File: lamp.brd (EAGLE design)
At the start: 184.2 x 38.1 mm, 63 parts, among them P1 10kΩ, P2 2MΩ

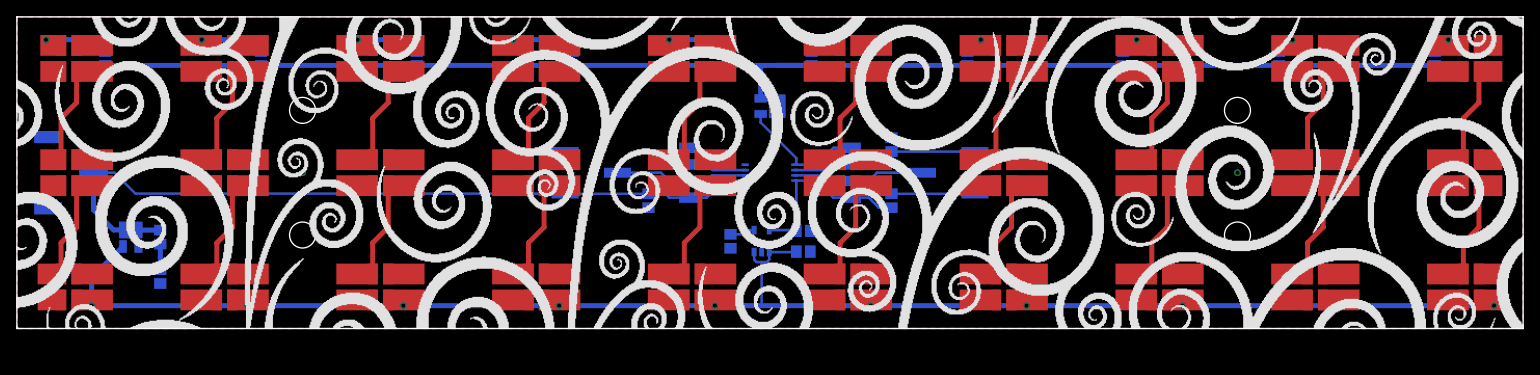
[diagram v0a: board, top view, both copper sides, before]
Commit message: Fixed nfet that controls led channels. Added resistors to pwm control line. Adjusted nfet and pfet symbols.
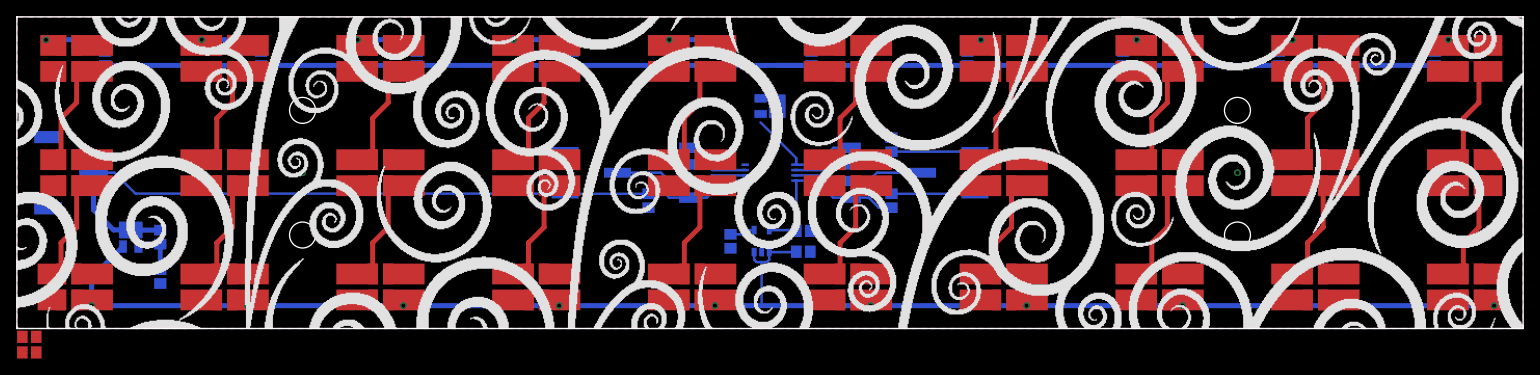
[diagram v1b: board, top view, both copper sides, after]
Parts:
- added R14: 100Ω, Barebones-Arduino:0805
- added R15: 100kΩ, Barebones-Arduino:0805
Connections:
- new net N$15: F1.P$1, R14.2, R15.2
- net GND: now also F1.S$2, R15.1; no longer F1.P$3
- net N$33: now also F1.P$3; no longer F1.S$2
- net N$47: now also R14.1; no longer F1.P$1
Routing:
- net N$33: track 170.7 -> 166.7 mm
- net N$47: track 15.8 -> 14.8 mm
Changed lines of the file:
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@@
 <layer number="29" name="tStop" color="7" fill="3" visible="yes" active="yes"/>
 <layer number="30" name="bStop" color="7" fill="6" visible="yes" active="yes"/>
-<layer number="31" name="tCream" color="7" fill="4" visible="no" active="yes"/>
-<layer number="32" name="bCream" color="7" fill="5" visible="no" active="yes"/>
+<layer number="31" name="tCream" color="7" fill="4" visible="yes" active="yes"/>
+<layer number="32" name="bCream" color="7" fill="5" visible="yes" active="yes"/>
 <layer number="33" name="tFinish" color="6" fill="3" visible="no" active="yes"/>
 <layer number="34" name="bFinish" color="6" fill="6" visible="no" active="yes"/>
@@
 </class>
 </classes>
-<designrules name="LaenPCBOrder *">
+<designrules name="LaenPCBOrder">
 <description language="de">&lt;b&gt;EAGLE Design Rules&lt;/b&gt;
 &lt;p&gt;
@@
 <param name="mvStopFrame" value="1"/>
 <param name="mvCreamFrame" value="0"/>
-<param name="mlMinStopFrame" value="5mil"/>
-<param name="mlMaxStopFrame" value="5mil"/>
+<param name="mlMinStopFrame" value="3mil"/>
+<param name="mlMaxStopFrame" value="3mil"/>
 <param name="mlMinCreamFrame" value="0mil"/>
 <param name="mlMaxCreamFrame" value="0mil"/>
-<param name="mlViaStopLimit" value="26mil"/>
+<param name="mlViaStopLimit" value="0mil"/>
 <param name="srRoundness" value="0"/>
 <param name="srMinRoundness" value="0mil"/>
@@
 <element name="C5" library=" Barebones-Arduino" package="0805" value="1µF" x="17.526" y="11.176" rot="MR270"/>
 <element name="F1" library="lamp" package="SOT-23-3" value="SI2318DS" x="92.075" y="27.178" smashed="yes" rot="MR90"/>
+<element name="R14" library=" Barebones-Arduino" package="0805" value="100Ω" x="1.524" y="-1.016"/>
+<element name="R15" library=" Barebones-Arduino" package="0805" value="100kΩ" x="1.524" y="-2.921"/>
 </elements>
 <signals>
@@
 <contactref element="U$3" pad="P$2"/>
 <wire x1="178.7525" y1="27.6225" x2="176.8475" y2="25.7175" width="0.6096" layer="1"/>
-<wire x1="176.8475" y1="20.6375" x2="176.8475" y2="25.7175" width="0.6096" layer="1"/>
+<wire x1="176.8475" y1="25.7175" x2="176.8475" y2="20.6375" width="0.6096" layer="1"/>
 <wire x1="178.7525" y1="27.6225" x2="178.7525" y2="31.4325" width="0.6096" layer="1"/>
 </signal>
@@
 <via x="155.956" y="35.306" extent="1-16" drill="0.5"/>
 <wire x1="157.7975" y1="35.306" x2="155.956" y2="35.306" width="0.6096" layer="1"/>
-<wire x1="157.7975" y1="34.6075" x2="157.7975" y2="35.306" width="0.6096" layer="1"/>
+<wire x1="157.7975" y1="35.306" x2="157.7975" y2="34.6075" width="0.6096" layer="1"/>
 </signal>
 <signal name="N$6">
@@
 <contactref element="U$8" pad="P$2"/>
 <wire x1="140.6525" y1="12.3825" x2="138.7475" y2="10.4775" width="0.6096" layer="1"/>
-<wire x1="138.7475" y1="10.4775" x2="138.7475" y2="6.6675" width="0.6096" layer="1"/>
+<wire x1="138.7475" y1="6.6675" x2="138.7475" y2="10.4775" width="0.6096" layer="1"/>
 <wire x1="140.6525" y1="12.3825" x2="140.6525" y2="17.4625" width="0.6096" layer="1"/>
 </signal>
@@
 <via x="136.906" y="35.306" extent="1-16" drill="0.5"/>
 <wire x1="138.7475" y1="35.306" x2="136.906" y2="35.306" width="0.6096" layer="1"/>
-<wire x1="138.7475" y1="34.6075" x2="138.7475" y2="35.306" width="0.6096" layer="1"/>
+<wire x1="138.7475" y1="35.306" x2="138.7475" y2="34.6075" width="0.6096" layer="1"/>
 </signal>
 <signal name="N$9">
@@
 <contactref element="U$9" pad="P$2"/>
 <wire x1="140.6525" y1="27.6225" x2="138.7475" y2="25.7175" width="0.6096" layer="1"/>
-<wire x1="138.7475" y1="20.6375" x2="138.7475" y2="25.7175" width="0.6096" layer="1"/>
+<wire x1="138.7475" y1="25.7175" x2="138.7475" y2="20.6375" width="0.6096" layer="1"/>
 <wire x1="140.6525" y1="27.6225" x2="140.6525" y2="31.4325" width="0.6096" layer="1"/>
 </signal>
@@
 <contactref element="U$11" pad="P$2"/>
 <wire x1="121.6025" y1="12.3825" x2="119.6975" y2="10.4775" width="0.6096" layer="1"/>
-<wire x1="121.6025" y1="17.4625" x2="121.6025" y2="12.3825" width="0.6096" layer="1"/>
+<wire x1="121.6025" y1="12.3825" x2="121.6025" y2="17.4625" width="0.6096" layer="1"/>
 <wire x1="119.6975" y1="10.4775" x2="119.6975" y2="6.6675" width="0.6096" layer="1"/>
 </signal>
@@
 <via x="117.856" y="35.306" extent="1-16" drill="0.5"/>
 <wire x1="119.6975" y1="35.306" x2="117.856" y2="35.306" width="0.6096" layer="1"/>
-<wire x1="119.6975" y1="34.6075" x2="119.6975" y2="35.306" width="0.6096" layer="1"/>
+<wire x1="119.6975" y1="35.306" x2="119.6975" y2="34.6075" width="0.6096" layer="1"/>
 </signal>
 <signal name="N$12">
@@
 <contactref element="U$14" pad="P$2"/>
 <wire x1="102.5525" y1="12.3825" x2="100.6475" y2="10.4775" width="0.6096" layer="1"/>
-<wire x1="102.5525" y1="17.4625" x2="102.5525" y2="12.3825" width="0.6096" layer="1"/>
 <wire x1="100.6475" y1="10.4775" x2="100.6475" y2="6.6675" width="0.6096" layer="1"/>
+<wire x1="102.5525" y1="12.3825" x2="102.5525" y2="17.4625" width="0.6096" layer="1"/>
 </signal>
 <signal name="N$32">
@@
 <via x="98.806" y="35.306" extent="1-16" drill="0.5"/>
 <wire x1="100.6475" y1="35.306" x2="98.806" y2="35.306" width="0.6096" layer="1"/>
-<wire x1="100.6475" y1="34.6075" x2="100.6475" y2="35.306" width="0.6096" layer="1"/>
+<wire x1="100.6475" y1="35.306" x2="100.6475" y2="34.6075" width="0.6096" layer="1"/>
 </signal>
 <signal name="N$13">
@@
 <contactref element="C4" pad="2"/>
 <contactref element="R13" pad="1"/>
-<contactref element="F1" pad="P$3"/>
 <contactref element="R12" pad="2"/>
+<contactref element="F1" pad="S$2"/>
+<contactref element="R15" pad="1"/>
+<wire x1="106.934" y1="23.329" x2="149.225" y2="19.05" width="0" layer="19" extent="16-16"/>
+<wire x1="96.989" y1="11.938" x2="106.934" y2="23.329" width="0" layer="19" extent="16-16"/>
+<wire x1="96.989" y1="9.398" x2="96.989" y2="11.938" width="0" layer="19" extent="16-16"/>
+<wire x1="91.059" y1="9.348" x2="96.989" y2="9.398" width="0" layer="19" extent="16-16"/>
+<wire x1="87.249" y1="9.818" x2="91.059" y2="9.348" width="0" layer="19" extent="16-16"/>
+<wire x1="89.045" y1="20.025" x2="87.249" y2="9.818" width="0" layer="19" extent="16-16"/>
+<wire x1="82.2325" y1="22.098" x2="89.045" y2="20.025" width="0" layer="19" extent="16-16"/>
+<wire x1="90.925" y1="28.128" x2="89.045" y2="20.025" width="0" layer="19" extent="16-16"/>
+<wire x1="77.216" y1="14.771" x2="82.2325" y2="22.098" width="0" layer="19" extent="16-16"/>
+<wire x1="34.925" y1="19.05" x2="77.216" y2="14.771" width="0" layer="19" extent="16-16"/>
+<wire x1="17.526" y1="5.5" x2="34.925" y2="19.05" width="0" layer="19" extent="16-16"/>
+<wire x1="9.37" y1="21.05" x2="17.526" y2="5.5" width="0" layer="19" extent="16-16"/>
+<wire x1="0.674" y1="-2.921" x2="17.526" y2="5.5" width="0" layer="19" extent="1-16"/>
 </signal>
 <signal name="N$18">
@@
 <contactref element="UC" pad="P$5"/>
 <contactref element="PB0" pad="1"/>
-<contactref element="F1" pad="P$1"/>
 <wire x1="101.9175" y1="22.098" x2="99.822" y2="22.098" width="0.3048" layer="16"/>
 <wire x1="99.822" y1="22.098" x2="97.749" y2="20.025" width="0.3048" layer="16"/>
@@
 <wire x1="95.289" y1="20.025" x2="95.289" y2="20.828" width="0.3048" layer="16"/>
 <wire x1="95.289" y1="20.828" x2="90.925" y2="25.192" width="0.3048" layer="16"/>
-<wire x1="90.925" y1="25.192" x2="90.925" y2="26.228" width="0.3048" layer="16"/>
+<contactref element="R14" pad="1"/>
+<wire x1="0.674" y1="-1.016" x2="90.925" y2="25.192" width="0" layer="19" extent="1-16"/>
 </signal>
 <signal name="N$46">
@@
 <wire x1="91.059" y1="8.128" x2="91.059" y2="2.794" width="0.3048" layer="16"/>
 <wire x1="91.059" y1="2.794" x2="88.9" y2="2.794" width="0.3048" layer="16"/>
+<wire x1="178.816" y1="3.429" x2="178.816" y2="2.794" width="0.6096" layer="1"/>
 <wire x1="102.5525" y1="3.4925" x2="102.5525" y2="2.794" width="0.6096" layer="1"/>
-<wire x1="159.7025" y1="3.4925" x2="159.7025" y2="2.794" width="0.6096" layer="1"/>
-<wire x1="140.6525" y1="3.4925" x2="140.6525" y2="2.794" width="0.6096" layer="1"/>
 <wire x1="121.6025" y1="3.4925" x2="121.6025" y2="2.794" width="0.6096" layer="1"/>
+<wire x1="140.6525" y1="3.4925" x2="140.6525" y2="2.794" width="0.6096" layer="1"/>
+<wire x1="159.7025" y1="3.4925" x2="159.7025" y2="2.794" width="0.6096" layer="1"/>
 <wire x1="178.7525" y1="3.4925" x2="178.816" y2="3.4925" width="0.6096" layer="1"/>
-<wire x1="178.816" y1="3.4925" x2="178.816" y2="2.794" width="0.6096" layer="1"/>
+<wire x1="178.816" y1="3.4925" x2="178.816" y2="3.429" width="0.6096" layer="1"/>
 </signal>
 <signal name="N$50">
@@
 <wire x1="90.925" y1="32.17" x2="86.995" y2="32.17" width="0.6096" layer="16"/>
 <wire x1="97.155" y1="32.17" x2="93.025" y2="32.17" width="0.6096" layer="16"/>
-<contactref element="F1" pad="S$2"/>
-<wire x1="90.925" y1="28.128" x2="90.925" y2="32.17" width="0.6096" layer="16"/>
 <wire x1="90.925" y1="32.17" x2="91.44" y2="32.17" width="0.6096" layer="16"/>
+<contactref element="F1" pad="P$3"/>
+<wire x1="93.025" y1="32.17" x2="92.95" y2="27.178" width="0" layer="19" extent="16-16"/>
 </signal>
 <signal name="+12V">
@@
 <wire x1="84.328" y1="20.066" x2="82.2325" y2="20.066" width="0.3048" layer="16"/>
 </signal>
+<signal name="N$15">
+<contactref element="R14" pad="2"/>
+<contactref element="R15" pad="2"/>
+<contactref element="F1" pad="P$1"/>
+<wire x1="2.374" y1="-1.016" x2="90.925" y2="26.228" width="0" layer="19" extent="1-16"/>
+<wire x1="2.374" y1="-2.921" x2="2.374" y2="-1.016" width="0" layer="19" extent="1-1"/>
+</signal>
 </signals>

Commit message: Removed soft-start RC from reverse polarity protection fet F2. Removed solder mask holes from led vias so they will get tented instead.
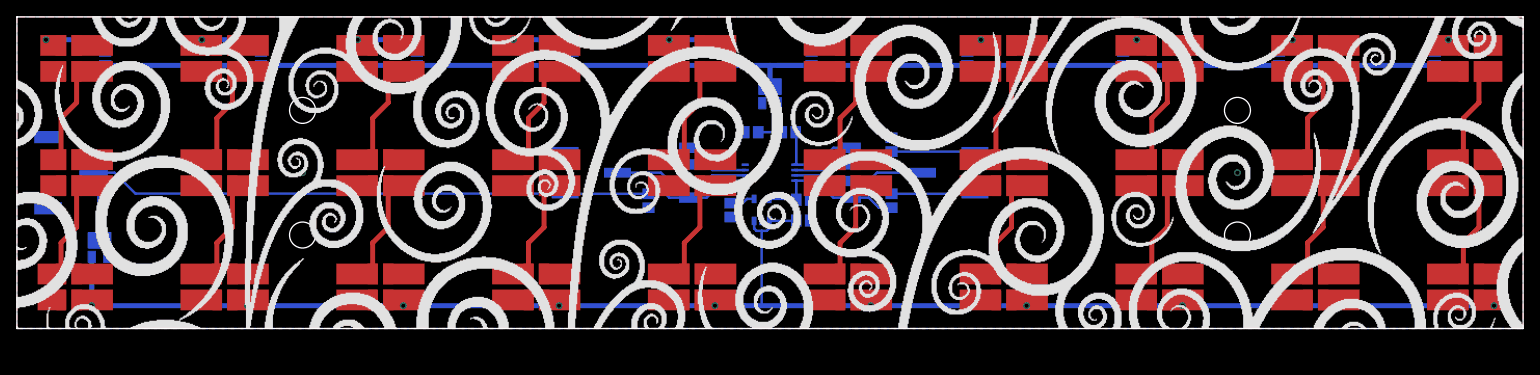
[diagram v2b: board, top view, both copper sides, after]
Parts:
- removed C5: 1µF, Barebones-Arduino:0805
- removed R15: 100kΩ, Barebones-Arduino:0805
- R13: value 10kΩ -> 100Ω
- R14: value 100Ω -> 100kΩ
- moved R14 91.7 mm to (89.8, 24.0), flipped to the bottom, turned to 180 degrees
- moved R13 78.8 mm to (94.4, 24.0), turned to 0 degrees
- moved F2 4.02 mm to (10.1, 9.91)
- moved C1 3.81 mm to (96.1, 13.2)
- moved C3 3.81 mm to (87.2, 14.5)
- moved VR 3.81 mm to (91.1, 14.5)
- moved C2 3.81 mm to (96.1, 15.7)
- moved F1 1.52 mm to (92.1, 28.7), turned to 0 degrees
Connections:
- removed net N$14: C5.2, F2.P$1, R13.2
- net +12V: no longer C5.1
- net GND: now also F2.P$1, R14.1; no longer R13.1, R15.1
- net N$15: now also R13.2; no longer R15.2
- net N$47: now also R13.1; no longer R14.1
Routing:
- net N$15: track 0.00 -> 6.62 mm
- net N$14: track 5.91 -> 0.00 mm
- net +12V: track 11.7 -> 7.01 mm
- net +5V: track 22.9 -> 19.1 mm
- net N$47: track 14.8 -> 11.8 mm
- net N$33: track 166.7 -> 169.3 mm
- net N$45: track 220.5 -> 221.5 mm
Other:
- board text added: "R14"
- board text removed: "C5"

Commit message: Various changes, I forget. Probably mostly artsy-fartsy silkscreen stuff.
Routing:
- net N$7: track 11.6 -> 12.7 mm
- net N$31: track 11.6 -> 12.7 mm
- net N$28: track 11.6 -> 12.7 mm
- net N$22: track 11.6 -> 12.7 mm
- net N$19: track 11.6 -> 12.7 mm
- net N$16: track 11.6 -> 12.7 mm
- net N$10: track 11.6 -> 12.7 mm
- net N$1: track 11.6 -> 12.7 mm
- net N$9: track 11.6 -> 12.7 mm
- net N$40: track 11.6 -> 12.7 mm
- net N$32: track 11.6 -> 12.7 mm
- net N$30: track 11.6 -> 12.7 mm
- net N$3: track 11.6 -> 12.7 mm
- net N$25: track 11.6 -> 12.7 mm
- net N$24: track 11.6 -> 12.7 mm
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- removed copper zone on layer 1, net GND
